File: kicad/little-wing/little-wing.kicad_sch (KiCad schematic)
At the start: 47 parts, among them J1 HRO_TYPE-C-31-M-14, J2 Battery, J3 rgb, J4 columns, J5 Conn_01x10, J6 rows, J7 sensor, Q1 AO3401A, Q2 2N7002, SW1 Battery, SW2 Reset, U1 BQ24075, U2 nRF52840_E73-2G4M08S1C, Y1 32.768 KHz

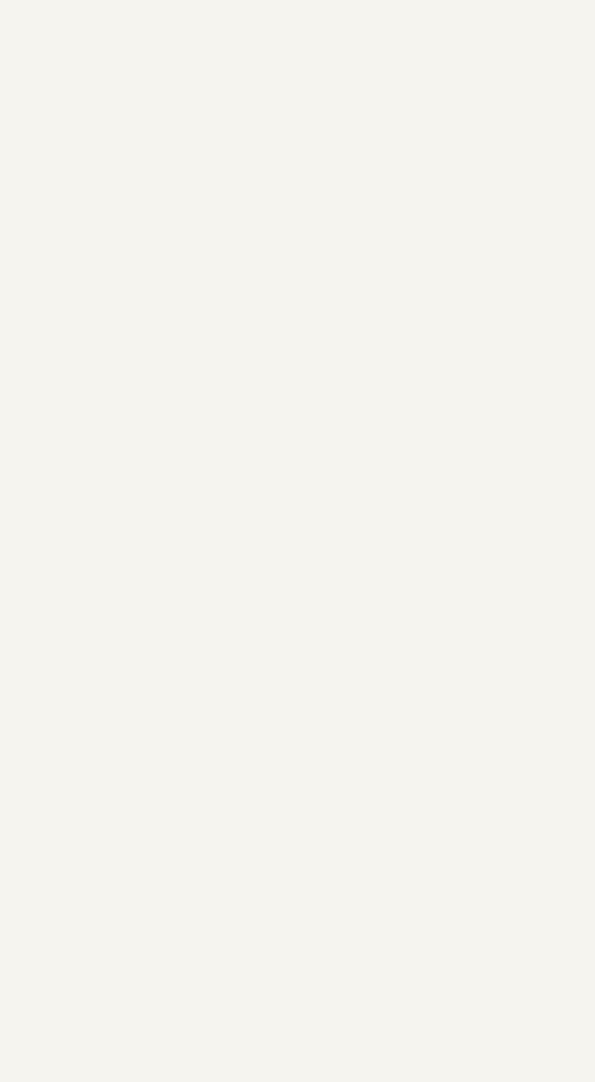
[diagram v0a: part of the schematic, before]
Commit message: Importing reference schematics for nrf52840 and npm1100 chips and renaming the project
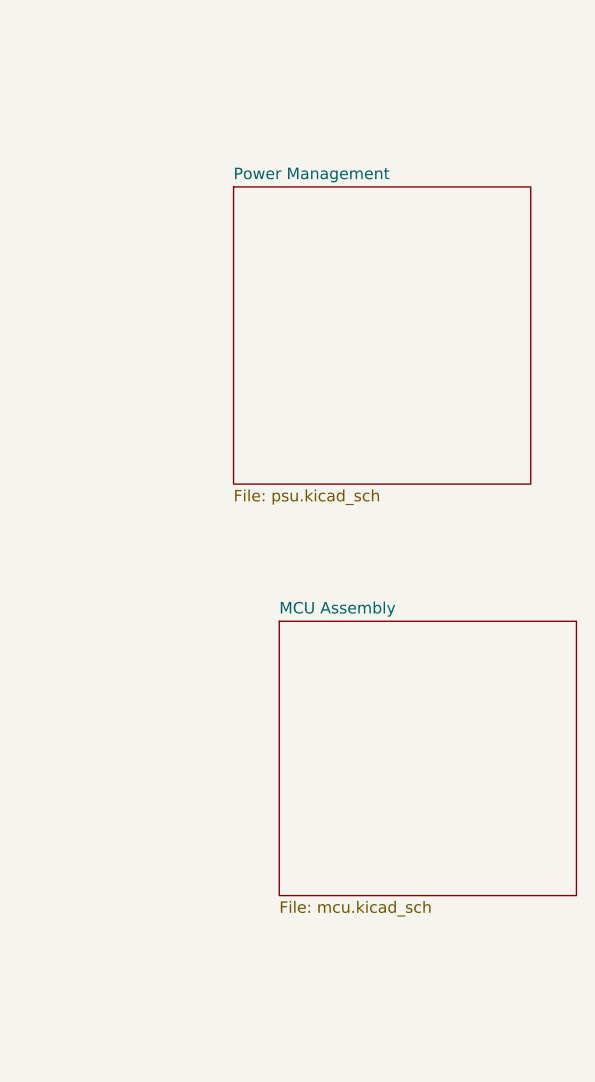
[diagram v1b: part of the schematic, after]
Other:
- added sheet MCU Assembly (mcu.kicad_sch)
- added sheet Power Management (psu.kicad_sch)
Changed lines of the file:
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@@
 				)
 				(justify right)
-				(hide yes)
 			)
 		)
@@
 				)
 				(justify right)
-				(hide yes)
 			)
 		)
@@
 				)
 				(justify left)
-				(hide yes)
 			)
 		)
@@
 				)
 				(justify left)
-				(hide yes)
 			)
 		)
@@
 				)
 				(justify left)
-				(hide yes)
 			)
 		)
@@
 				)
 				(justify right)
-				(hide yes)
 			)
 		)
@@
 				)
 				(justify right)
-				(hide yes)
 			)
 		)
@@
 				)
 				(justify right)
-				(hide yes)
 			)
 		)
@@
 				)
 				(justify right)
-				(hide yes)
 			)
 		)
@@
 				)
 				(justify right)
-				(hide yes)
 			)
 		)
@@
 				)
 				(justify right)
-				(hide yes)
 			)
 		)
@@
 				)
 				(justify left)
-				(hide yes)
 			)
 		)
@@
 				)
 				(justify right)
-				(hide yes)
 			)
 		)
@@
 				)
 				(justify right)
-				(hide yes)
 			)
 		)
@@
 				)
 				(justify right)
-				(hide yes)
 			)
 		)
@@
 				)
 				(justify right)
-				(hide yes)
 			)
 		)
@@
 				)
 				(justify right)
-				(hide yes)
 			)
 		)
@@
 				)
 				(justify right)
-				(hide yes)
 			)
 		)
@@
 				)
 				(justify right)
-				(hide yes)
 			)
 		)
@@
 				)
 				(justify left)
-				(hide yes)
 			)
 		)
@@
 				)
 				(justify left)
-				(hide yes)
 			)
 		)
@@
 				)
 				(justify right)
-				(hide yes)
 			)
 		)
@@
 				)
 				(justify right)
-				(hide yes)
 			)
 		)
@@
 				)
 				(justify left)
-				(hide yes)
 			)
 		)
@@
 				)
 				(justify left)
-				(hide yes)
 			)
 		)
@@
 				)
 				(justify right)
-				(hide yes)
 			)
 		)
@@
 				)
 				(justify right)
-				(hide yes)
 			)
 		)
@@
 				)
 				(justify right)
-				(hide yes)
 			)
 		)
@@
 				)
 				(justify left)
-				(hide yes)
 			)
 		)
@@
 				)
 				(justify left)
-				(hide yes)
 			)
 		)
@@
 				)
 				(justify left)
-				(hide yes)
 			)
 		)
@@
 				)
 				(justify left)
-				(hide yes)
 			)
 		)
@@
 				)
 				(justify right)
-				(hide yes)
 			)
 		)
@@
 				)
 				(justify right)
-				(hide yes)
 			)
 		)
@@
 				)
 				(justify right)
-				(hide yes)
 			)
 		)
@@
 				)
 				(justify right)
-				(hide yes)
 			)
 		)
@@
 				)
 				(justify left)
-				(hide yes)
 			)
 		)
@@
 				)
 				(justify left)
-				(hide yes)
 			)
 		)
@@
 				)
 				(justify left)
-				(hide yes)
 			)
 		)
@@
 				)
 				(justify right)
-				(hide yes)
 			)
 		)
@@
 				)
 				(justify right)
-				(hide yes)
 			)
 		)
@@
 				)
 				(justify right)
-				(hide yes)
 			)
 		)
@@
 				)
 				(justify right)
-				(hide yes)
 			)
 		)
@@
 				)
 				(justify left)
-				(hide yes)
 			)
 		)
@@
 				)
 				(justify right)
-				(hide yes)
 			)
 		)
@@
 				)
 				(justify right)
-				(hide yes)
 			)
 		)
@@
 				)
 				(justify left)
-				(hide yes)
 			)
 		)
@@
 				)
 				(justify left)
-				(hide yes)
 			)
 		)
@@
 				)
 				(justify right)
-				(hide yes)
 			)
 		)
@@
 				)
 				(justify right)
-				(hide yes)
 			)
 		)
@@
 				)
 				(justify right)
-				(hide yes)
 			)
 		)
@@
 				)
 				(justify right)
-				(hide yes)
 			)
 		)
@@
 				)
 				(justify right)
-				(hide yes)
 			)
 		)
@@
 				)
 				(justify right)
-				(hide yes)
 			)
 		)
@@
 				)
 				(justify right)
-				(hide yes)
 			)
 		)
@@
 				)
 				(justify right)
-				(hide yes)
 			)
 		)
@@
 				)
 				(justify left)
-				(hide yes)
 			)
 		)
@@
 				)
 			)
+		)
+	)
+	(sheet
+		(at 450.85 137.16)
+		(size 33.02 30.48)
+		(exclude_from_sim no)
+		(in_bom yes)
+		(on_board yes)
+		(dnp no)
+		(fields_autoplaced yes)
+		(stroke
+			(width 0.1524)
+			(type solid)
+		)
+		(fill
+			(color 0 0 0 0.0000)
+		)
+		(property "Sheetname" "MCU Assembly"
+			(at 450.85 136.4484 0)
+			(effects
+				(font
+					(size 1.27 1.27)
+				)
+				(justify left bottom)
+			)
+		)
+		(property "Sheetfile" "mcu.kicad_sch"
+			(at 450.85 168.2246 0)
+			(effects
+				(font
+					(size 1.27 1.27)
+				)
+				(justify left top)
+			)
+		)
+		(instances
+			(project "mobo"
+				(path "/3a835e6f-a660-4b38-a102-87841cdd95ed"
+					(page "3")
+				)
+			)
+		)
+	)
+	(sheet
+		(at 445.77 88.9)
+		(size 33.02 33.02)
+		(exclude_from_sim no)
+		(in_bom yes)
+		(on_board yes)
+		(dnp no)
+		(fields_autoplaced yes)
+		(stroke
+			(width 0.1524)
+			(type solid)
+		)
+		(fill
+			(color 0 0 0 0.0000)
+		)
+		(property "Sheetname" "Power Management"
+			(at 445.77 88.1884 0)
+			(effects
+				(font
+					(size 1.27 1.27)
+				)
+				(justify left bottom)
+			)
+		)
+		(property "Sheetfile" "psu.kicad_sch"
+			(at 445.77 122.5046 0)
+			(effects
+				(font
+					(size 1.27 1.27)
+				)
+				(justify left top)
+			)
+		)
+		(instances
+			(project "mobo"
+				(path "/3a835e6f-a660-4b38-a102-87841cdd95ed"
+					(page "2")
+				)
+			)

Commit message: Re-shuffling the schematics across sub-sheets
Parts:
- removed C1, C2, C3, C5, C6: 4u7, Capacitor_SMD:C_0402_1005Metric, symbol Device:C_Small
- removed C10, C8: 1uF, Capacitor_SMD:C_0603_1608Metric_Pad1.08x0.95mm_HandSolder, symbol Device:C_Small
- removed C11, C9: 12p, Capacitor_SMD:C_0402_1005Metric, symbol Device:C_Small
- removed C4: 1u, Capacitor_SMD:C_0402_1005Metric, symbol Device:C_Small
- removed C7: 560pF/680pF, Capacitor_SMD:C_0603_1608Metric_Pad1.08x0.95mm_HandSolder, symbol Device:C_Small
- removed FB1, FB2: 2.7k, Resistor_SMD:R_0805_2012Metric_Pad1.20x1.40mm_HandSolder, symbol sharp_memory_display-rescue:Ferrite_Bead_Small-Device
- removed J1: HRO_TYPE-C-31-M-14, Connector_USB:USB_C_Receptacle_HRO_TYPE-C-31-M-12, symbol Connector:USB_C_Receptacle_USB2.0
- removed J2: Battery, Connector_JST:JST_SH_SM02B-SRSS-TB_1x02-1MP_P1.00mm_Horizontal, symbol Connector_Generic:Conn_01x02
- removed J3: rgb, Connector_JST:JST_SH_SM03B-SRSS-TB_1x03-1MP_P1.00mm_Horizontal, symbol Connector:Conn_01x03_Socket
- removed J4: columns, Connector_JST:JST_SH_SM06B-SRSS-TB_1x06-1MP_P1.00mm_Horizontal, symbol Connector:Conn_01x06_Socket
- removed J5: Conn_01x10, Connector_FFC-FPC:Hirose_FH12-10S-0.5SH_1x10-1MP_P0.50mm_Horizontal, symbol Connector_Generic:Conn_01x10
- removed J6: rows, Connector_JST:JST_SH_SM05B-SRSS-TB_1x05-1MP_P1.00mm_Horizontal, symbol Connector:Conn_01x05_Socket
- removed J7: sensor, Connector_JST:JST_SH_SM06B-SRSS-TB_1x06-1MP_P1.00mm_Horizontal, symbol Connector:Conn_01x06_Socket
- removed L1: 10 uH, Inductor_SMD:L_0603_1608Metric, symbol Device:L_Small
- removed LED1: orange, LED_SMD:LED_0402_1005Metric, symbol Device:LED_Small
- removed Q1: AO3401A, Package_TO_SOT_SMD:SOT-23, symbol Transistor_FET:AO3401A
- removed Q2: 2N7002, Package_TO_SOT_SMD:SOT-23, symbol Transistor_FET:2N7002
- removed R1, R2: 5k1, Resistor_SMD:R_0402_1005Metric, symbol Device:R_Small
- removed R10, R18, R3: 10k, Resistor_SMD:R_0402_1005Metric, symbol Device:R_Small
- removed R11, R14, R15, R16, R17, R8: 100R, Resistor_SMD:R_0402_1005Metric, symbol Device:R_Small
- removed R12, R13, R9: 10k, Resistor_SMD:R_0603_1608Metric_Pad0.98x0.95mm_HandSolder, symbol Device:R_Small
- removed R4, R6: 1k5, Resistor_SMD:R_0402_1005Metric, symbol Device:R_Small
- removed R5: 47k, Resistor_SMD:R_0402_1005Metric, symbol Device:R_Small
- removed R7: 3k9, Resistor_SMD:R_0402_1005Metric, symbol Device:R_Small
- removed SW1: Battery, symbol Switch:SW_SPST
- removed SW2: Reset, Button_Switch_SMD:SW_SPST_B3U-1000P, symbol ScottoKeebs:Placeholder_Switch
- removed U1: BQ24075, Package_DFN_QFN:VQFN-16-1EP_3x3mm_P0.5mm_EP1.6x1.6mm, symbol Battery_Management:BQ24075RGT
- removed U2: nRF52840_E73-2G4M08S1C, E73-2G4M08S1C Model:E73-2G4M08S1C, symbol PCM_marbastlib-various:nRF52840_E73-2G4M08S1C
- removed Y1: 32.768 KHz, Crystal:Crystal_SMD_2012-2Pin_2.0x1.2mm, symbol Device:Crystal_Small
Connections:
- no-connect marks 5 -> 0
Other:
- removed sheet MCU Assembly
- removed sheet Power Management
- added sheet Main Module (mobo.kicad_sch)
- added sheet old-backup (old-backup.kicad_sch)
- note removed: "Battery management"
- note removed: "External DCCH inductor for DC-DC HV input mode"
- note removed: "External LF crystal for lower idle power"
- note removed: "IO connectors"
- note removed: "LCD Screen"
- note removed: "MCU section"
- note removed: "USB connector"
- note removed: "Underglow power"

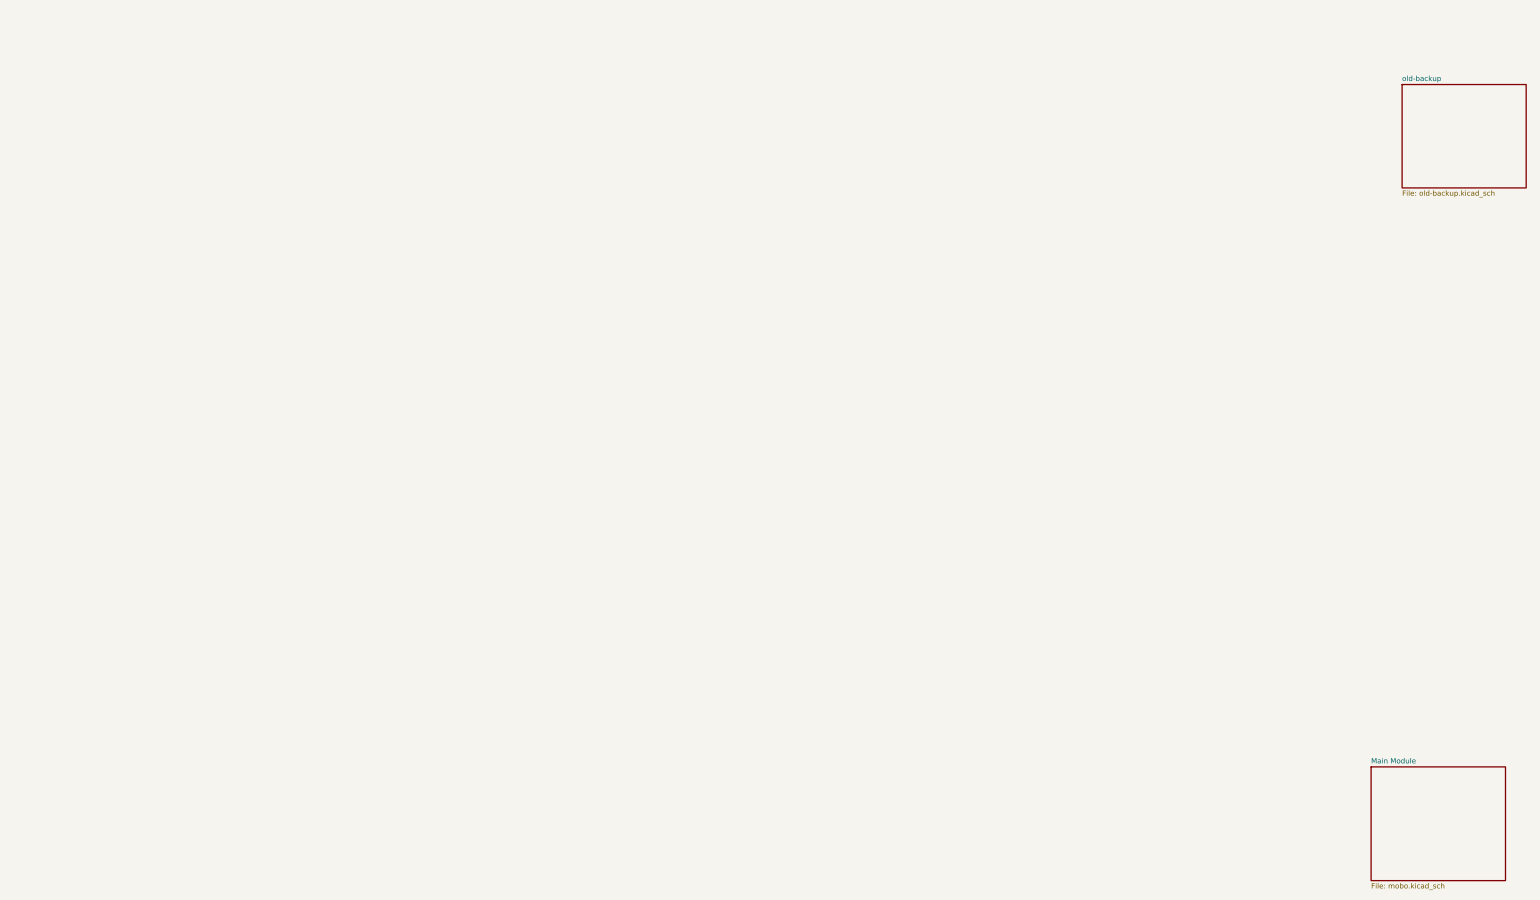
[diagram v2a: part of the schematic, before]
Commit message: Copying over the reference PCB stacks
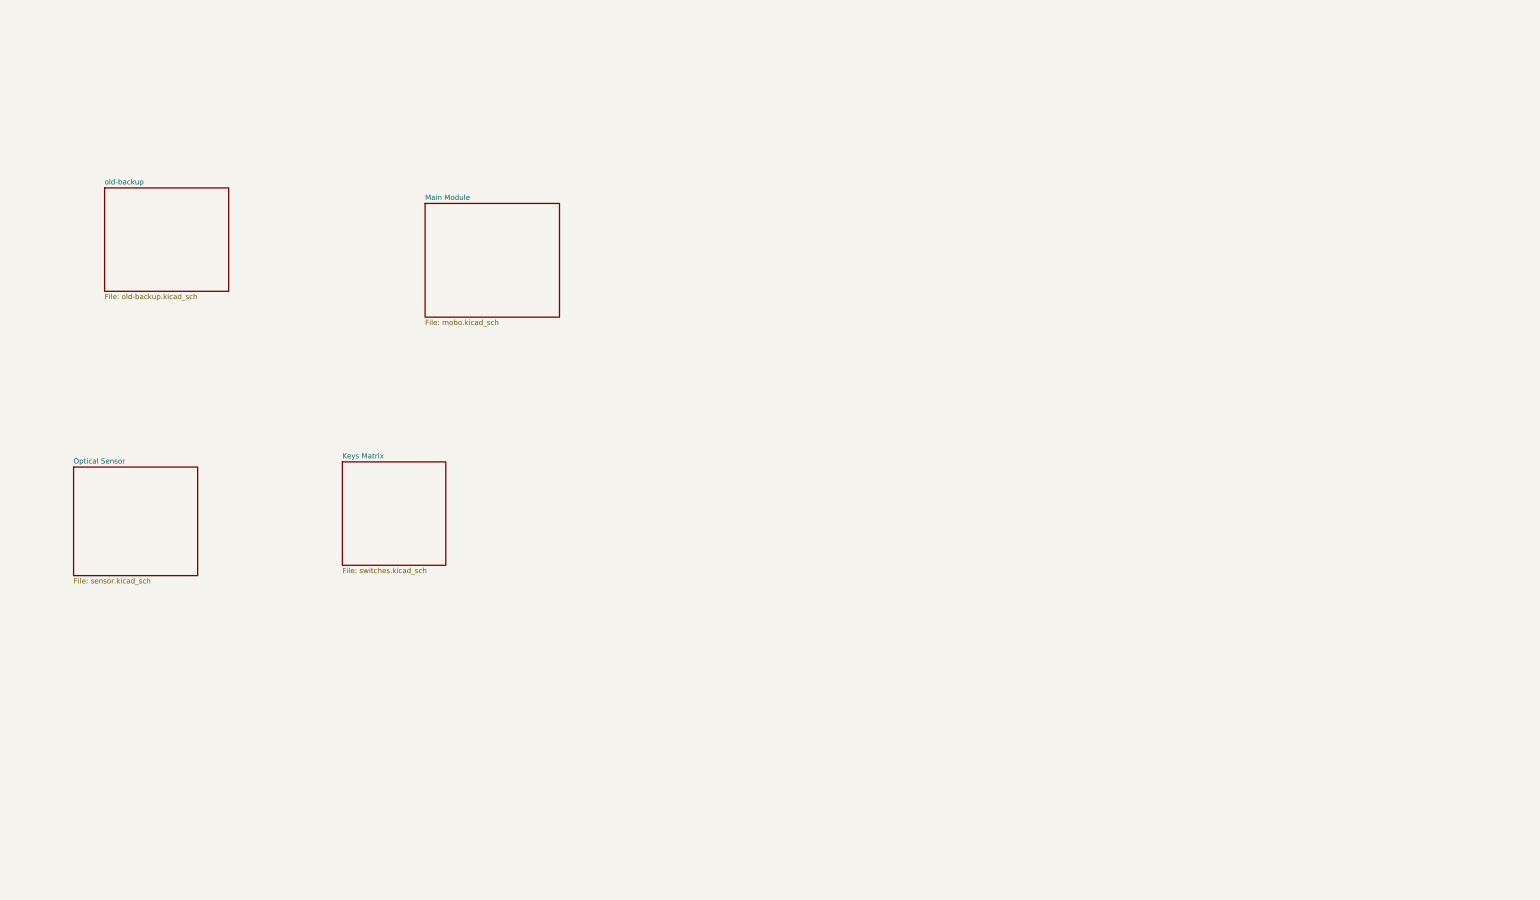
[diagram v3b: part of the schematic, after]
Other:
- added sheet Keys Matrix (switches.kicad_sch)
- added sheet Optical Sensor (sensor.kicad_sch)
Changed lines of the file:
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@@
 	)
 	(sheet
-		(at 453.39 24.13)
+		(at 134.62 49.53)
 		(size 30.48 25.4)
 		(exclude_from_sim no)
@@
 		)
 		(property "Sheetname" "old-backup"
-			(at 453.39 23.4184 0)
+			(at 134.62 48.8184 0)
 			(effects
 				(font
@@
 		)
 		(property "Sheetfile" "old-backup.kicad_sch"
-			(at 453.39 50.1146 0)
+			(at 134.62 75.5146 0)
 			(effects
 				(font
@@
 	)
 	(sheet
-		(at 445.77 191.77)
+		(at 127 118.11)
+		(size 30.48 26.67)
+		(exclude_from_sim no)
+		(in_bom yes)
+		(on_board yes)
+		(dnp no)
+		(fields_autoplaced yes)
+		(stroke
+			(width 0.1524)
+			(type solid)
+		)
+		(fill
+			(color 0 0 0 0.0000)
+		)
+		(property "Sheetname" "Optical Sensor"
+			(at 127 117.3984 0)
+			(effects
+				(font
+					(size 1.27 1.27)
+				)
+				(justify left bottom)
+			)
+		)
+		(property "Sheetfile" "sensor.kicad_sch"
+			(at 127 145.3646 0)
+			(effects
+				(font
+					(size 1.27 1.27)
+				)
+				(justify left top)
+			)
+		)
+		(instances
+			(project "little-wing"
+				(path "/3a835e6f-a660-4b38-a102-87841cdd95ed"
+					(page "8")
+				)
+			)
+		)
+	)
+	(sheet
+		(at 193.04 116.84)
+		(size 25.4 25.4)
+		(exclude_from_sim no)
+		(in_bom yes)
+		(on_board yes)
+		(dnp no)
+		(fields_autoplaced yes)
+		(stroke
+			(width 0.1524)
+			(type solid)
+		)
+		(fill
+			(color 0 0 0 0.0000)
+		)
+		(property "Sheetname" "Keys Matrix"
+			(at 193.04 116.1284 0)
+			(effects
+				(font
+					(size 1.27 1.27)
+				)
+				(justify left bottom)
+			)
+		)
+		(property "Sheetfile" "switches.kicad_sch"
+			(at 193.04 142.8246 0)
+			(effects
+				(font
+					(size 1.27 1.27)
+				)
+				(justify left top)
+			)
+		)
+		(instances
+			(project "little-wing"
+				(path "/3a835e6f-a660-4b38-a102-87841cdd95ed"
+					(page "9")
+				)
+			)
+		)
+	)
+	(sheet
+		(at 213.36 53.34)
 		(size 33.02 27.94)
 		(exclude_from_sim no)
@@
 		)
 		(property "Sheetname" "Main Module"
-			(at 445.77 191.0584 0)
+			(at 213.36 52.6284 0)
 			(effects
 				(font
@@
 		)
 		(property "Sheetfile" "mobo.kicad_sch"
-			(at 445.77 220.2946 0)
+			(at 213.36 81.8646 0)
 			(effects
 				(font

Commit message: Tidying up the mess a little bit
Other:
- removed sheet old-backup
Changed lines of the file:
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@@
-	)
-	(sheet
-		(at 134.62 49.53)
-		(size 30.48 25.4)
-		(exclude_from_sim no)
-		(in_bom yes)
-		(on_board yes)
-		(dnp no)
-		(fields_autoplaced yes)
-		(stroke
-			(width 0.1524)
-			(type solid)
-		)
-		(fill
-			(color 0 0 0 0.0000)
-		)
-		(property "Sheetname" "old-backup"
-			(at 134.62 48.8184 0)
-			(effects
-				(font
-					(size 1.27 1.27)
-				)
-				(justify left bottom)
-			)
-		)
-		(property "Sheetfile" "old-backup.kicad_sch"
-			(at 134.62 75.5146 0)
-			(effects
-				(font
-					(size 1.27 1.27)
-				)
-				(justify left top)
-			)
-		)
-		(instances
-			(project "little-wing"
-				(path "/3a835e6f-a660-4b38-a102-87841cdd95ed"
-					(page "4")
-				)
-			)
-		)
 	)
 	(sheet
